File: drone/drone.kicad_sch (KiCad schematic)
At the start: 52 parts, among them J2 HMC5883, J3 Conn_01x03_Pin, SW1 SW_Push, SW2 SW_Push, U1 ESP32-WROOM-32D, U2 MPU-6050, U3 MP2303ADN

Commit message: hi
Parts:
- removed C5, C6: 220pF, Capacitor_SMD:C_0805_2012Metric_Pad1.18x1.45mm_HandSolder, symbol Device:C
- removed C7, C8: 0.1uF, Capacitor_SMD:C_0805_2012Metric_Pad1.18x1.45mm_HandSolder, symbol Device:C
- removed R3, R4: 4.7k, Resistor_SMD:R_0805_2012Metric_Pad1.20x1.40mm_HandSolder, symbol Device:R
- removed U2: MPU-6050, MPU-6050:QFN50P400X400X95-24N, symbol MPU-6050:MPU-6050
- added C4: 10nF, Capacitor_SMD:C_0805_2012Metric_Pad1.18x1.45mm_HandSolder, symbol Device:C
- added J1: Conn_01x04_Pin, Connector_PinSocket_2.54mm:PinSocket_1x04_P2.54mm_Vertical, symbol Connector:Conn_01x04_Pin
- H1, H2, H3, H4: footprint MountingHole:MountingHole_3.5mm -> MountingHole:MountingHole_3.2mm_M3
- TP10, TP3, TP4, TP5, TP6, TP7, TP8, TP9: footprint TestPoint:TestPoint_Pad_D2.5mm -> TestPoint:TestPoint_Pad_2.5x2.5mm
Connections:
- net +3V3: now also C4.1, J1.1 (Pin_1)
- net GND: now also C4.2, J1.2 (Pin_2)
- net SCL: now also J1.3 (Pin_3)
- net SDA: now also J1.4 (Pin_4)
- no-connect marks 2 -> 0
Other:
- note added: "GY 87"
- note removed: "MPU6050"

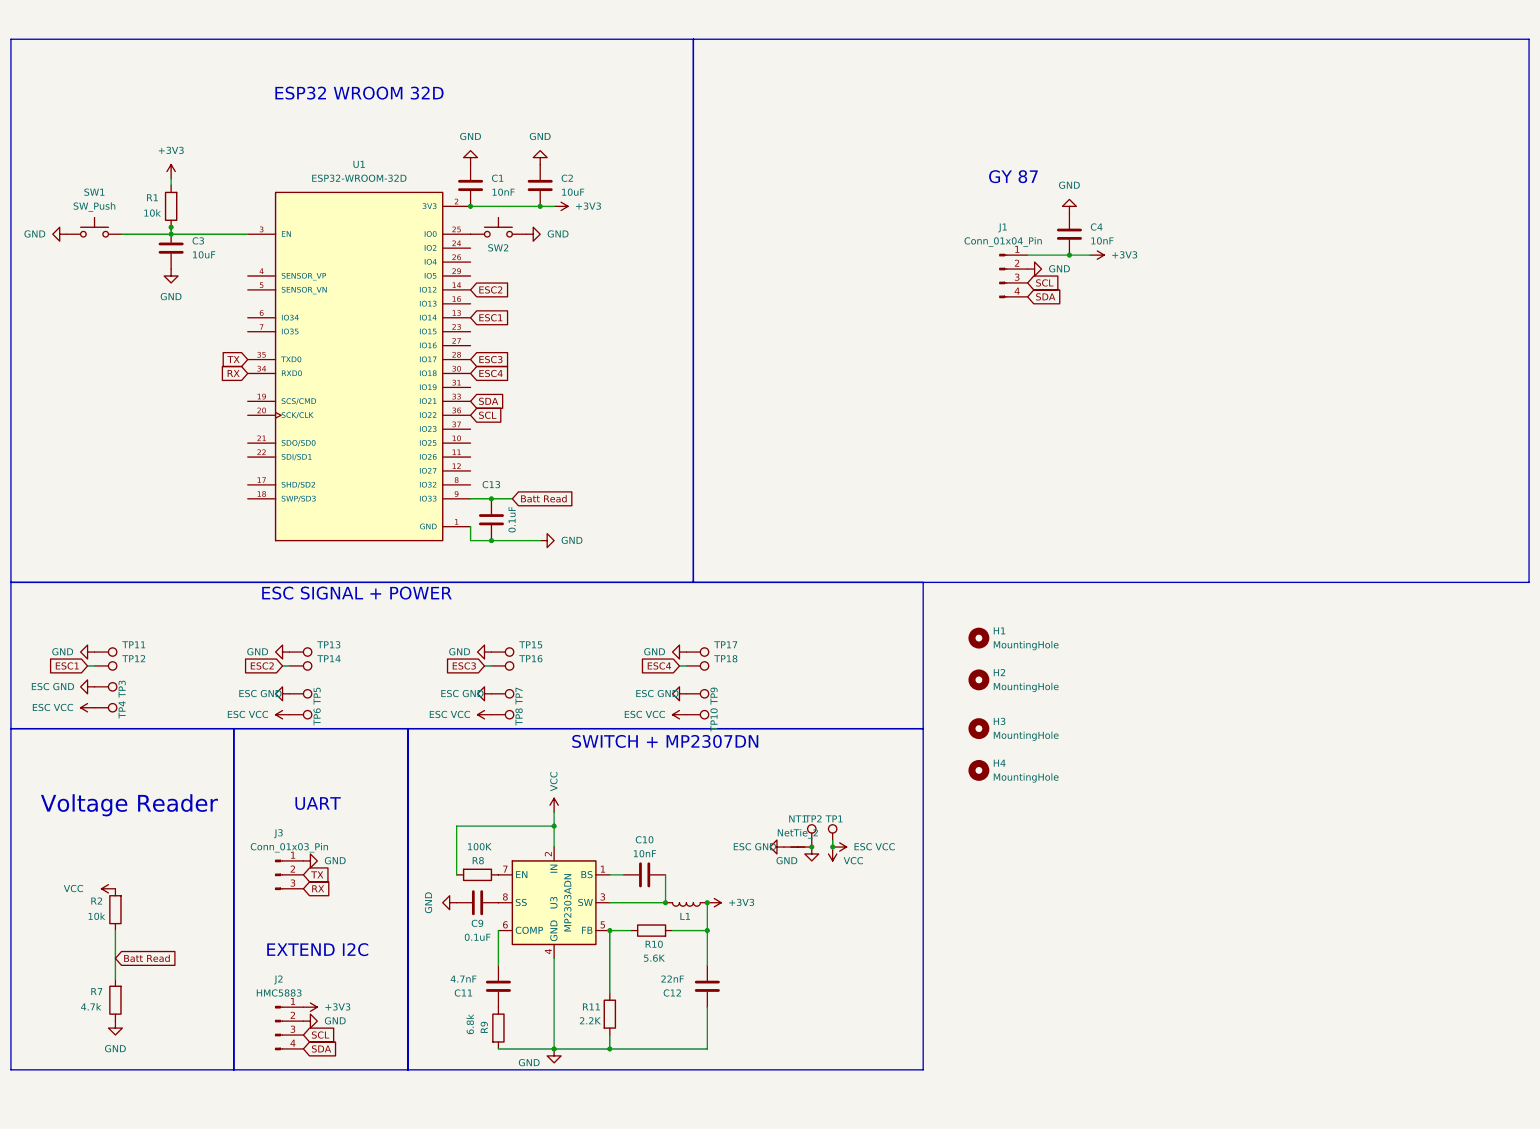
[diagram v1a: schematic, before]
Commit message: size 30.5 + esp32 s3 supermini
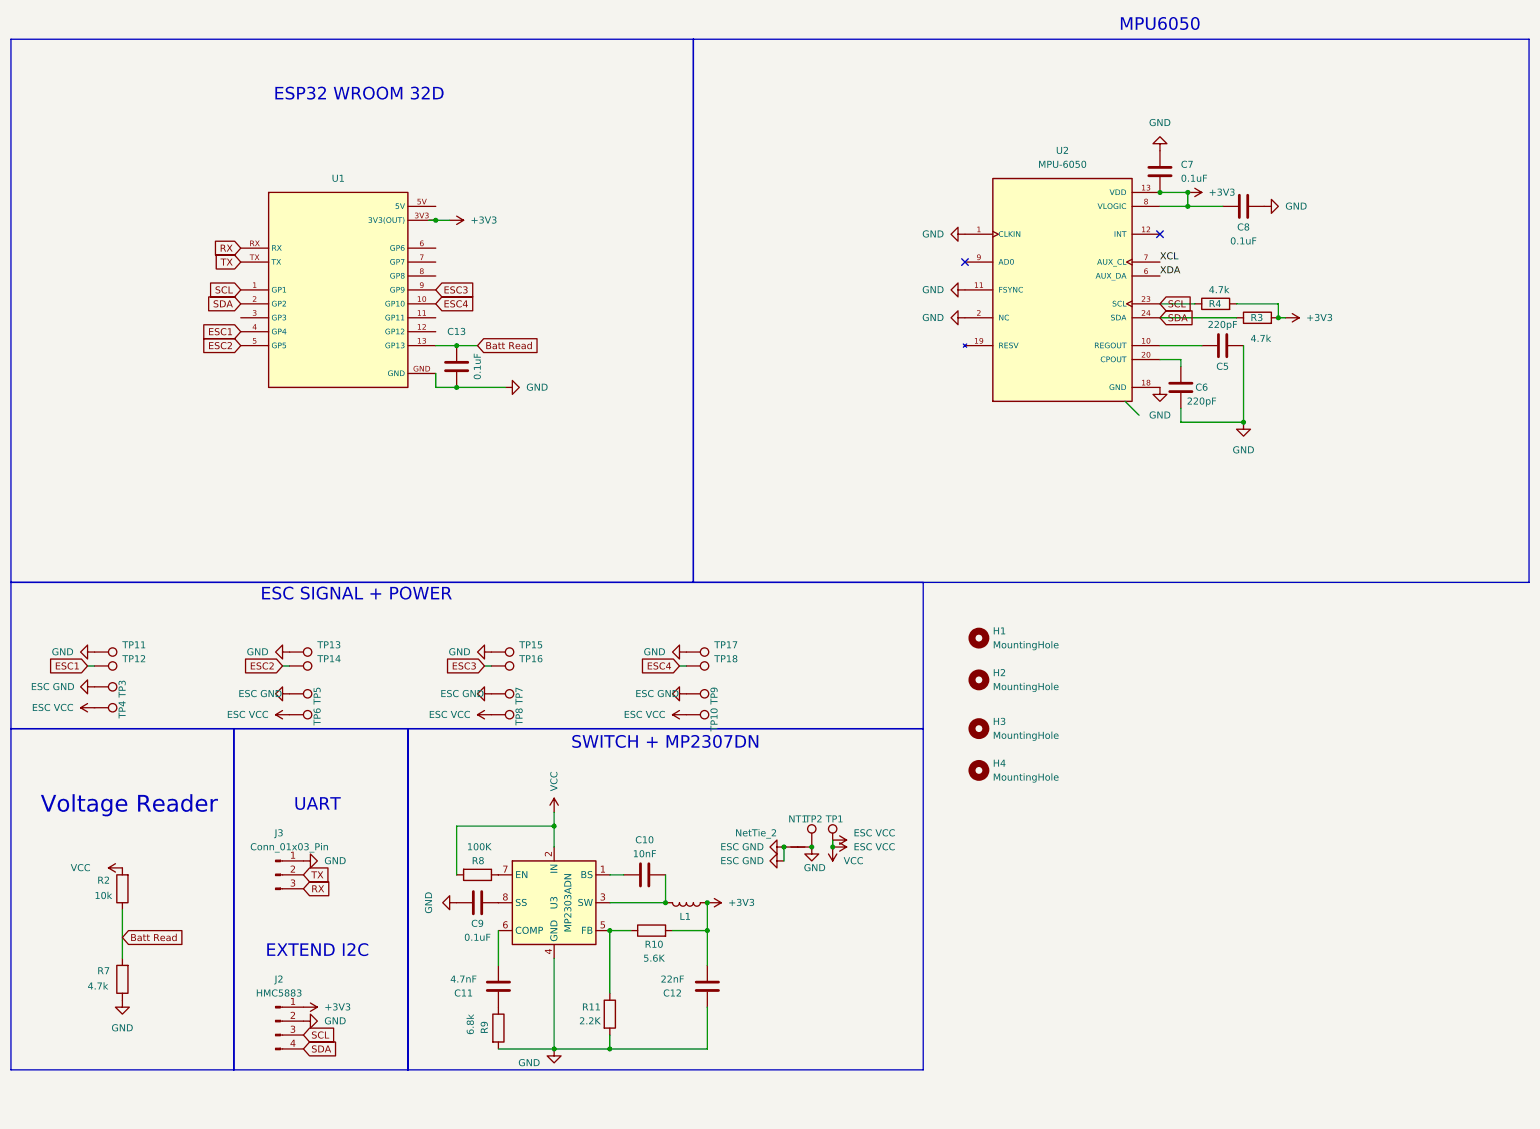
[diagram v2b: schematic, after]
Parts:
- removed C1, C4: 10nF, Capacitor_SMD:C_0805_2012Metric_Pad1.18x1.45mm_HandSolder, symbol Device:C
- removed C2, C3: 10uF, Capacitor_SMD:C_0805_2012Metric_Pad1.18x1.45mm_HandSolder, symbol Device:C
- removed J1: Conn_01x04_Pin, Connector_PinSocket_2.54mm:PinSocket_1x04_P2.54mm_Vertical, symbol Connector:Conn_01x04_Pin
- removed R1: 10k, Resistor_SMD:R_0805_2012Metric_Pad1.20x1.40mm_HandSolder, symbol Device:R
- removed SW1, SW2: SW_Push, Button_Switch_SMD:SW_SPST_TS-1088-xR025, symbol Switch:SW_Push
- removed U1: ESP32-WROOM-32D, ESP32-WROOM-32D:MODULE_ESP32-WROOM-32D, symbol ESP32-WROOM-32D:ESP32-WROOM-32D
- added C5, C6: 220pF, Capacitor_SMD:C_0805_2012Metric_Pad1.18x1.45mm_HandSolder, symbol Device:C
- added C7, C8: 0.1uF, Capacitor_SMD:C_0805_2012Metric_Pad1.18x1.45mm_HandSolder, symbol Device:C
- added R3, R4: 4.7k, Resistor_SMD:R_0805_2012Metric_Pad1.20x1.40mm_HandSolder, symbol Device:R
- added U1: (no value), ESP32-S3-Supermini:ESP32-S3-SuperMini, symbol ESP32-S3-Supermini:ESP32-S3-Supermini
- added U2: MPU-6050, MPU-6050:QFN50P400X400X95-24N, symbol MPU-6050:MPU-6050
- TP10, TP3, TP4, TP5, TP6, TP7, TP8, TP9: footprint TestPoint:TestPoint_Pad_2.5x2.5mm -> TestPoint:TestPoint_Pad_1.5x1.5mm
- TP11, TP12, TP13, TP14, TP15, TP16, TP17, TP18: footprint TestPoint:TestPoint_Pad_1.5x1.5mm -> TestPoint:TestPoint_Pad_1.0x1.0mm
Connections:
- net +3V3: now also C7.2, C8.2, R3.2, R4.2, U1.3V3 (3V3(OUT)), U2.13 (VDD), U2.8 (VLOGIC)
- net Batt Read: now also U1.13 (GP13)
- net ESC1: now also U1.4 (GP4)
- net ESC2: now also U1.5 (GP5)
- net ESC3: now also U1.9 (GP9)
- net ESC4: now also U1.10 (GP10)
- net GND: now also C5.2, C6.2, C7.1, C8.1, U1.GND, U2.1 (CLKIN), U2.11 (FSYNC), U2.14 (NC), U2.15 (NC), U2.16 (NC), U2.17 (NC), U2.18 (GND), U2.2 (NC), U2.3 (NC), U2.4 (NC), U2.5 (NC)
- net RX: now also U1.RX
- net SCL: now also R4.1, U1.1 (GP1), U2.23 (SCL)
- net SDA: now also R3.1, U1.2 (GP2), U2.24 (SDA)
- net TX: now also U1.TX
- new net: C5.1, U2.10 (REGOUT)
- new net: U2.19 (RESV), U2.21 (RESV), U2.22 (RESV)
- new net: C6.1, U2.20 (CPOUT)
- new net XDA: U2.6 (AUX_DA)
- no-connect marks 0 -> 2
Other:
- note added: "MPU6050"
- note removed: "GY 87"
- moved on the sheet: C13, R2, R7

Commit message: ho
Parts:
- added TP19, TP20: TestPoint, TestPoint:TestPoint_Pad_2.5x2.5mm, symbol Connector:TestPoint
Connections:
- net ESC VCC: now also TP20.1
- net GND: now also TP19.1
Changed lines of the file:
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@@
 	)
 	(junction
-		(at 151.13 157.48)
-		(diameter 0)
-		(color 0 0 0 0)
-	)
-	(junction
 		(at 224.79 38.1)
 		(diameter 0)
@@
 	(wire
 		(pts
+			(xy 149.86 157.48) (xy 151.13 157.48)
+		)
+		(stroke
+			(width 0)
+			(type default)
+		)
+	)
+	(wire
+		(pts
 			(xy 95.25 66.04) (xy 91.44 66.04)
 		)
@@
 	(wire
 		(pts
+			(xy 156.21 161.29) (xy 156.21 157.48)
+		)
+		(stroke
+			(width 0)
+			(type default)
+		)
+	)
+	(wire
+		(pts
 			(xy 231.14 40.64) (xy 224.79 40.64)
 		)
@@
 	(wire
 		(pts
-			(xy 234.95 66.04) (xy 234.95 80.01)
+			(xy 149.86 161.29) (xy 156.21 161.29)
 		)
 		(stroke
@@
 	(wire
 		(pts
-			(xy 100.33 73.66) (xy 91.44 73.66)
+			(xy 234.95 66.04) (xy 234.95 80.01)
 		)
 		(stroke
@@
 	(wire
 		(pts
-			(xy 223.52 80.01) (xy 223.52 77.47)
+			(xy 100.33 73.66) (xy 91.44 73.66)
 		)
 		(stroke
@@
 	(wire
 		(pts
-			(xy 91.44 66.04) (xy 87.63 66.04)
+			(xy 223.52 80.01) (xy 223.52 77.47)
 		)
 		(stroke
@@
 	(wire
 		(pts
-			(xy 119.38 172.72) (xy 123.19 172.72)
+			(xy 91.44 66.04) (xy 87.63 66.04)
 		)
 		(stroke
@@
 	(wire
 		(pts
-			(xy 151.13 157.48) (xy 151.13 160.02)
+			(xy 119.38 172.72) (xy 123.19 172.72)
 		)
 		(stroke
@@
 	)
 	(symbol
-		(lib_id "power:GND")
-		(at 151.13 160.02 270)
-		(unit 1)
-		(body_style 1)
-		(exclude_from_sim no)
-		(in_bom yes)
-		(on_board yes)
-		(in_pos_files yes)
-		(dnp no)
-		(property "Reference" "#PWR044"
-			(at 144.78 160.02 0)
-			(hide yes)
-			(show_name no)
-			(do_not_autoplace no)
-			(effects
-				(font
-					(size 1.27 1.27)
-				)
-			)
-		)
-		(property "Value" "ESC GND"
-			(at 143.51 160.02 90)
-			(show_name no)
-			(do_not_autoplace no)
-			(effects
-				(font
-					(size 1.27 1.27)
-				)
-			)
-		)
-		(property "Footprint" ""
-			(at 151.13 160.02 0)
-			(hide yes)
-			(show_name no)
-			(do_not_autoplace no)
-			(effects
-				(font
-					(size 1.27 1.27)
-				)
-			)
-		)
-		(property "Datasheet" ""
-			(at 151.13 160.02 0)
-			(hide yes)
-			(show_name no)
-			(do_not_autoplace no)
-			(effects
-				(font
-					(size 1.27 1.27)
-				)
-			)
-		)
-		(property "Description" "Power symbol creates a global label with name \"GND\" , ground"
-			(at 151.13 160.02 0)
-			(hide yes)
-			(show_name no)
-			(do_not_autoplace no)
-			(effects
-				(font
-					(size 1.27 1.27)
-				)
-			)
-		)
-		(pin "1"
-		)
-		(instances
-			(project "drone"
-				(path "/fa7edb3b-7a08-4951-b563-6ccff1e89ead"
-					(reference "#PWR044")
-					(unit 1)
-				)
-			)
-		)
-	)
-	(symbol
 		(lib_id "power:VCC")
 		(at 30.48 161.29 90)
@@
 	)
 	(symbol
+		(lib_id "Connector:TestPoint")
+		(at 149.86 161.29 90)
+		(unit 1)
+		(body_style 1)
+		(exclude_from_sim no)
+		(in_bom yes)
+		(on_board yes)
+		(in_pos_files yes)
+		(dnp no)
+		(property "Reference" "TP19"
+			(at 144.78 162.56 0)
+			(show_name no)
+			(do_not_autoplace no)
+			(effects
+				(font
+					(size 1.27 1.27)
+				)
+				(justify left)
+			)
+		)
+		(property "Value" "TestPoint"
+			(at 147.8279 158.75 0)
+			(hide yes)
+			(show_name no)
+			(do_not_autoplace no)
+			(effects
+				(font
+					(size 1.27 1.27)
+				)
+				(justify left)
+			)
+		)
+		(property "Footprint" "TestPoint:TestPoint_Pad_2.5x2.5mm"
+			(at 149.86 156.21 0)
+			(hide yes)
+			(show_name no)
+			(do_not_autoplace no)
+			(effects
+				(font
+					(size 1.27 1.27)
+				)
+			)
+		)
+		(property "Datasheet" ""
+			(at 149.86 156.21 0)
+			(hide yes)
+			(show_name no)
+			(do_not_autoplace no)
+			(effects
+				(font
+					(size 1.27 1.27)
+				)
+			)
+		)
+		(property "Description" "test point"
+			(at 149.86 161.29 0)
+			(hide yes)
+			(show_name no)
+			(do_not_autoplace no)
+			(effects
+				(font
+					(size 1.27 1.27)
+				)
+			)
+		)
+		(pin "1"
+		)
+		(instances
+			(project "drone"
+				(path "/fa7edb3b-7a08-4951-b563-6ccff1e89ead"
+					(reference "TP19")
+					(unit 1)
+				)
+			)
+		)
+	)
+	(symbol
 		(lib_id "Device:C")
 		(at 99.06 182.88 0)
@@
 	)
 	(symbol
-		(lib_id "power:VCC")
-		(at 160.02 157.48 270)
-		(unit 1)
-		(body_style 1)
-		(exclude_from_sim no)
-		(in_bom yes)
-		(on_board yes)
-		(in_pos_files yes)
-		(dnp no)
-		(property "Reference" "#PWR043"
-			(at 156.21 157.48 0)
-			(hide yes)
-			(show_name no)
-			(do_not_autoplace no)
-			(effects
-				(font
-					(size 1.27 1.27)
-				)
-			)
-		)
-		(property "Value" "ESC VCC"
-			(at 167.64 157.48 90)
-			(show_name no)
-			(do_not_autoplace no)
-			(effects
-				(font
-					(size 1.27 1.27)
-				)
-			)
-		)
-		(property "Footprint" ""
-			(at 160.02 157.48 0)
-			(hide yes)
-			(show_name no)
-			(do_not_autoplace no)
-			(effects
-				(font
-					(size 1.27 1.27)
-				)
-			)
-		)
-		(property "Datasheet" ""
-			(at 160.02 157.48 0)
-			(hide yes)
-			(show_name no)
-			(do_not_autoplace no)
-			(effects
-				(font
-					(size 1.27 1.27)
-				)
-			)
-		)
-		(property "Description" "Power symbol creates a global label with name \"VCC\""
-			(at 160.02 157.48 0)
-			(hide yes)
-			(show_name no)
-			(do_not_autoplace no)
-			(effects
-				(font
-					(size 1.27 1.27)
-				)
-			)
-		)
-		(pin "1"
-		)
-		(instances
-			(project "drone"
-				(path "/fa7edb3b-7a08-4951-b563-6ccff1e89ead"
-					(reference "#PWR043")
-					(unit 1)
-				)
-			)
-		)
-	)
-	(symbol
 		(lib_id "Connector:TestPoint")
 		(at 160.02 157.48 0)
@@
 					(unit 1)
 				)
+			)
+		)
+	)
+	(symbol
+		(lib_id "Connector:TestPoint")
+		(at 160.02 157.48 270)
+		(unit 1)
+		(body_style 1)
+		(exclude_from_sim no)
+		(in_bom yes)
+		(on_board yes)
+		(in_pos_files yes)
+		(dnp no)
+		(property "Reference" "TP20"
+			(at 165.1 156.21 0)
+			(show_name no)
+			(do_not_autoplace no)
+			(effects
+				(font
+					(size 1.27 1.27)
+				)
+				(justify left)
+			)
+		)
+		(property "Value" "TestPoint"
+			(at 162.0521 160.02 0)
+			(hide yes)
+			(show_name no)
+			(do_not_autoplace no)
+			(effects
+				(font
+					(size 1.27 1.27)
+				)
+				(justify left)
+			)
+		)
+		(property "Footprint" "TestPoint:TestPoint_Pad_2.5x2.5mm"
+			(at 160.02 162.56 0)
+			(hide yes)
+			(show_name no)
+			(do_not_autoplace no)
+			(effects
+				(font
+					(size 1.27 1.27)
+				)
+			)
+		)
+		(property "Datasheet" ""
+			(at 160.02 162.56 0)
+			(hide yes)
+			(show_name no)
+			(do_not_autoplace no)
+			(effects
+				(font
+					(size 1.27 1.27)
+				)
+			)
+		)
+		(property "Description" "test point"
+			(at 160.02 157.48 0)
+			(hide yes)
+			(show_name no)
+			(do_not_autoplace no)
+			(effects
+				(font
+					(size 1.27 1.27)
+				)
+			)
+		)
+		(pin "1"
+		)
+		(instances
+			(project "drone"
+				(path "/fa7edb3b-7a08-4951-b563-6ccff1e89ead"
+					(reference "TP20")
+					(unit 1)
+				)

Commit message: drc 0
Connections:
- net Batt Read: now also U1.8 (GP8); no longer U1.13 (GP13)
- net ESC GND: now also C12.2, C9.2, R11.2, R9.2, TP11.1, TP13.1, TP15.1, TP17.1, U3.4 (GND)
- net ESC3: now also U1.10 (GP10); no longer U1.9 (GP9)
- net ESC4: now also U1.9 (GP9); no longer U1.10 (GP10)
- net GND: no longer C12.2, C9.2, R11.2, R9.2, TP11.1, TP13.1, TP15.1, TP17.1, U3.4 (GND)
- net SCL: now also U1.12 (GP12); no longer U1.1 (GP1)
- net SDA: now also U1.11 (GP11); no longer U1.2 (GP2)
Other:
- moved on the sheet: C13

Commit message: add buzzer
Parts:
- added +Buzzer1, -Buzzer1: TestPoint, TestPoint:TestPoint_Pad_1.0x1.0mm, symbol Connector:TestPoint
- added Q1: AO3400A, Package_TO_SOT_SMD:SOT-23, symbol Transistor_FET:AO3400A
- renumbered TP4 to +1, TP6 to +2, TP8 to +3, TP10 to +4, TP3 to -1, TP5 to -2, TP7 to -3, TP9 to -4, TP12 to ESC1, TP14 to ESC2, TP16 to ESC3, TP18 to ESC4, TP11 to LED1, TP15 to LED2, TP17 to LED3, TP13 to TPLED1
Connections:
- net +3V3: now also +Buzzer1.1
- net GND: now also Q1.2 (S)
- net Buzzer: now reaches U1.13 (GP13)
- net Buzzer: now also Q1.1 (G)
- new net: -Buzzer1.1, Q1.3 (D)
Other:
- note added: "Indicators"
- moved on the sheet: TP20
